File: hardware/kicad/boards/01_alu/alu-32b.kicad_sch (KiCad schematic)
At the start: 0 parts

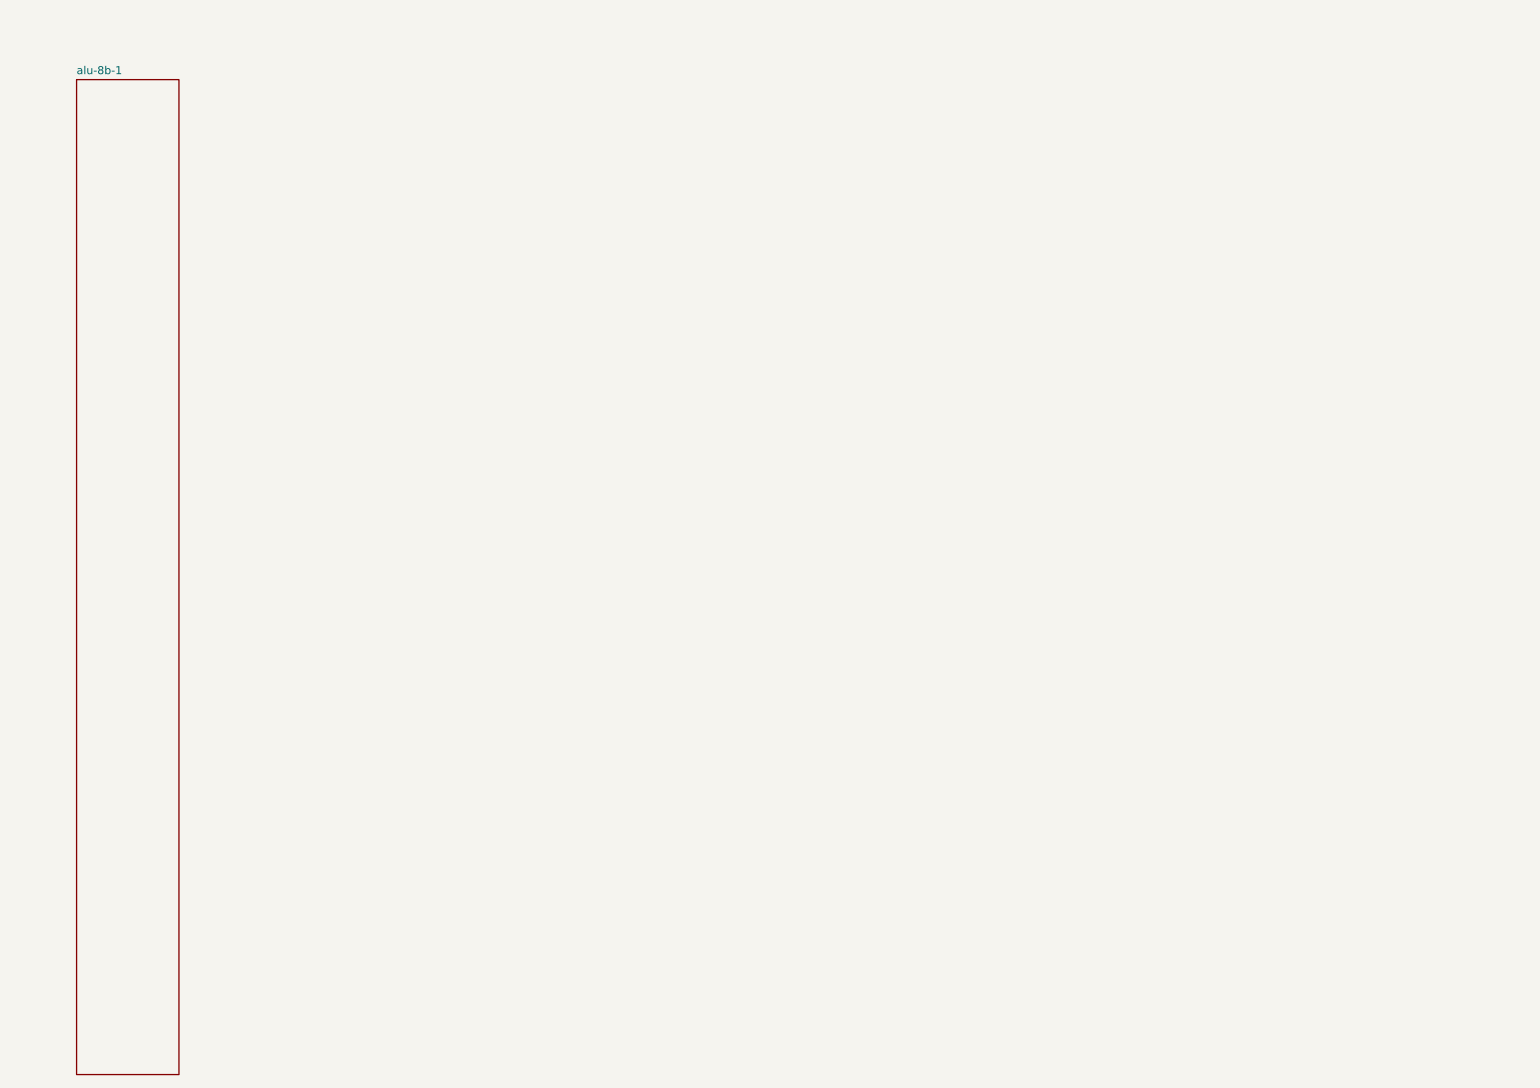
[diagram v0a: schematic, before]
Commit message: feat: designed alu0-control unit and wired on top level of 32b alu
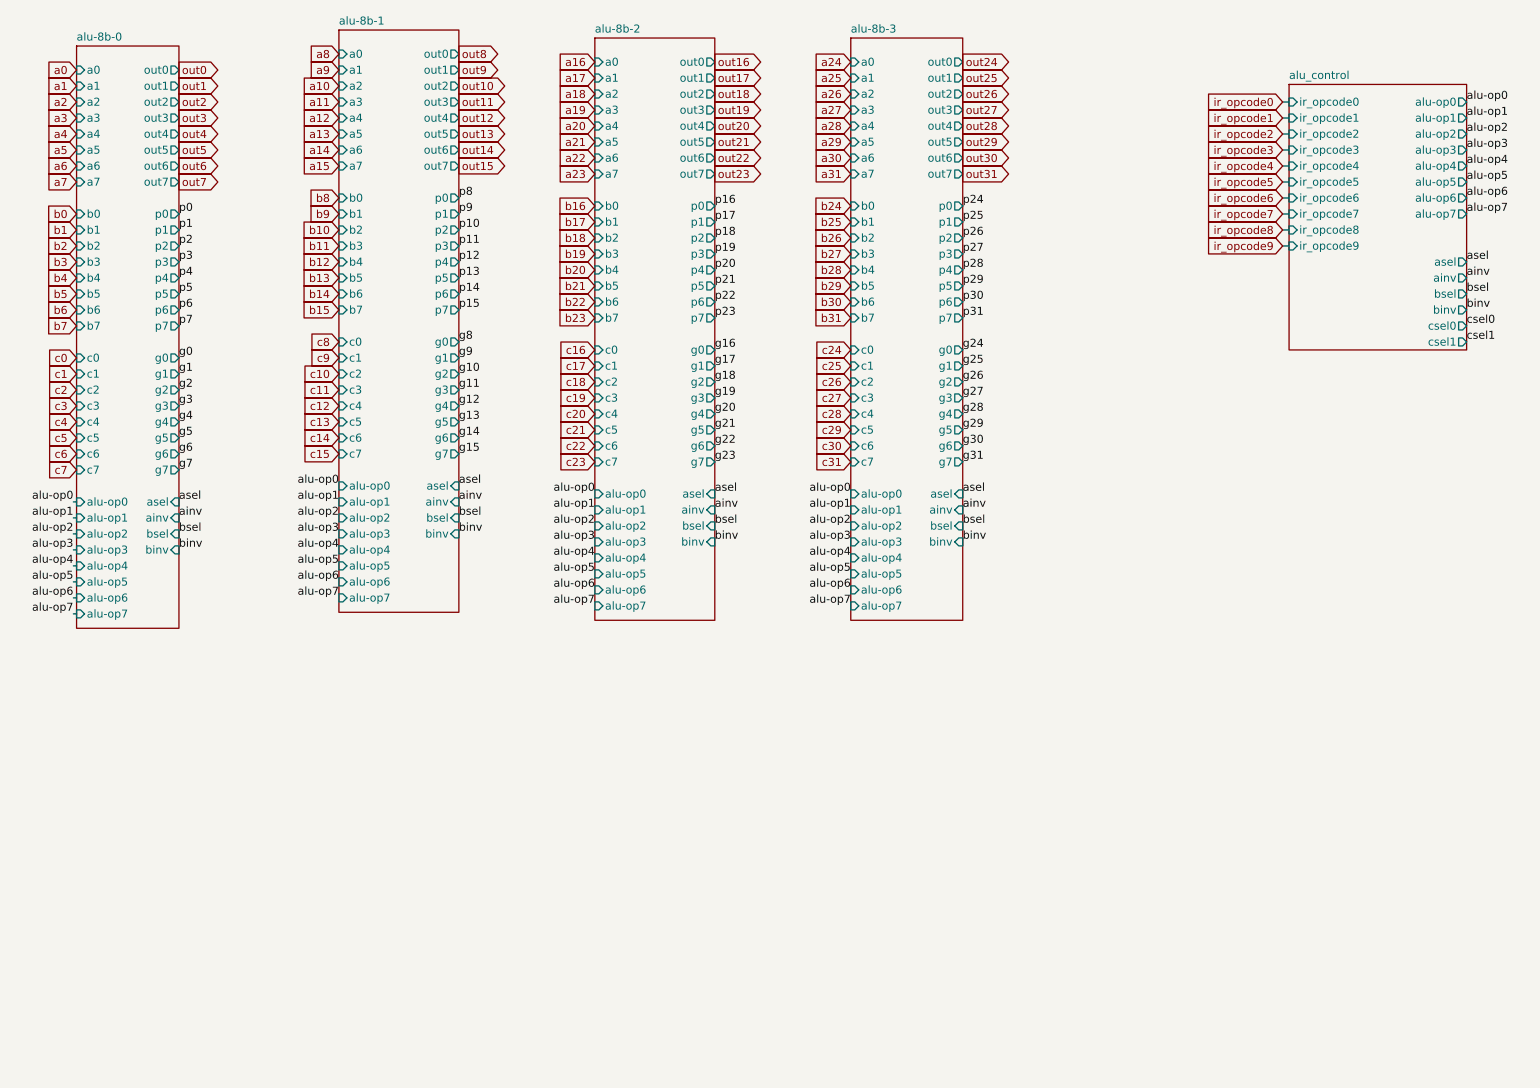
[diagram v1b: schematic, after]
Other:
- added sheet alu-8b-0 (alu-8b.kicad_sch)
- added sheet alu-8b-2 (alu-8b.kicad_sch)
- added sheet alu-8b-3 (alu-8b.kicad_sch)
- added sheet alu_control (alu_control.kicad_sch)
- sheet alu-8b-1 ports: added a0, a1, a2, a3, a4, a5, a6, a7, ainv, alu-op0, alu-op1, alu-op2, alu-op3, alu-op4, alu-op5, alu-op6, alu-op7, asel, b0, b1, b2, b3, b4, b5, b6, b7, binv, bsel, c0, c1, c2, c3, c4, c5, c6, c7, g0, g1, g2, g3, g4, g5, g6, g7, out0, out1, out2, out3, out4, out5, out6, out7, p0, p1, p2, p3, p4, p5, p6, p7; removed none

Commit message: kicad: checkpoint; designed the alu display logic; clock circuit
Added registers for each display to ensure robustness and less worry about debugging screen, keeping focus on the alu board and other components
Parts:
- added C1, C10, C11, C12, C13, C14, C15, C16, C17, C18, C19, C2, C20, C205, C206, C21, C22, C23, C24, C25, C26, C27, C28, C29, C3, C30, C4, C5, C6, C7, C8, C9: 100nF, Capacitor_SMD:C_0805_2012Metric, symbol Device:C
- added J1, J2, J3, J4: Conn_02x16_Odd_Even, Connector_PinHeader_2.54mm:PinHeader_2x16_P2.54mm_Vertical, symbol Connector_Generic:Conn_02x16_Odd_Even
- added J6: Conn_02x07_Odd_Even, Connector_PinHeader_2.54mm:PinHeader_2x07_P2.54mm_Vertical, symbol Connector_Generic:Conn_02x07_Odd_Even
- added U1, U10, U13, U14, U16, U18, U21, U4, U5, U6, U9: 74LS182, Package_DIP:DIP-16_W7.62mm, symbol 74xx:74LS182
- added U11, U12, U19, U2, U20, U27, U3, U7, U8: 74LS540, Package_SO:SOIC-20W_7.5x12.8mm_P1.27mm, symbol 74xx:74LS540
- added U15: 74LS153, Package_SO:SOIC-16_3.9x9.9mm_P1.27mm, symbol 74xx:74LS153
- added U17: 74AHCT1G08, Package_TO_SOT_SMD:SOT-23-5, symbol 74xGxx:74AHCT1G08
- added U205, U206: 74AHC541, Package_SO:SOIC-20W_7.5x12.8mm_P1.27mm, symbol 74xx:74AHC541
- added U22, U28: 74LS377, Package_SO:SOIC-20W_7.5x12.8mm_P1.27mm, symbol 74xx:74LS377
- added U23: 74HC86, Package_SO:SOIC-14_3.9x8.7mm_P1.27mm, symbol 74xx:74HC86
- added U24, U25, U29, U30: 74LS30, Package_SO:SOIC-14_3.9x8.7mm_P1.27mm, symbol 74xx:74LS30
- added U26: 74HCT00, Package_SO:SOIC-14_3.9x8.7mm_P1.27mm, symbol 74xx:74HCT00
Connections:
- net a0: now also J1.1 (Pin_1)
- net a1: now also J1.2 (Pin_2)
- net a10: now also J1.11 (Pin_11)
- net a11: now also J1.12 (Pin_12)
- net a12: now also J1.13 (Pin_13)
- net a13: now also J1.14 (Pin_14)
- net a14: now also J1.15 (Pin_15)
- net a15: now also J1.16 (Pin_16)
- net a16: now also J1.17 (Pin_17)
- net a17: now also J1.18 (Pin_18)
- net a18: now also J1.19 (Pin_19)
- net a19: now also J1.20 (Pin_20)
- net a2: now also J1.3 (Pin_3)
- net a20: now also J1.21 (Pin_21)
- net a21: now also J1.22 (Pin_22)
- net a22: now also J1.23 (Pin_23)
- net a23: now also J1.24 (Pin_24)
- net a24: now also J1.25 (Pin_25)
- net a25: now also J1.26 (Pin_26)
- net a26: now also J1.27 (Pin_27)
- net a27: now also J1.28 (Pin_28)
- net a28: now also J1.29 (Pin_29)
- net a29: now also J1.30 (Pin_30)
- net a3: now also J1.4 (Pin_4)
- net a30: now also J1.31 (Pin_31)
- net a31: now also J1.32 (Pin_32)
- net a4: now also J1.5 (Pin_5)
- net a5: now also J1.6 (Pin_6)
- net a6: now also J1.7 (Pin_7)
- net a7: now also J1.8 (Pin_8)
- net a8: now also J1.9 (Pin_9)
- net a9: now also J1.10 (Pin_10)
- net ainv: now also U205.17 (Y1)
- net alu-op0: now also U206.18 (Y0)
- net alu-op1: now also U206.17 (Y1)
- net alu-op2: now also U206.16 (Y2)
- net alu-op3: now also U206.15 (Y3)
- net alu-op4: now also U206.14 (Y4)
- net alu-op5: now also U206.13 (Y5)
- net alu-op6: now also U206.12 (Y6)
- net alu-op7: now also U206.11 (Y7)
- net asel: now also U205.18 (Y0)
- net b0: now also J3.1 (Pin_1)
- net b1: now also J3.2 (Pin_2)
- net b10: now also J3.11 (Pin_11)
- net b11: now also J3.12 (Pin_12)
- net b12: now also J3.13 (Pin_13)
- net b13: now also J3.14 (Pin_14)
- net b14: now also J3.15 (Pin_15)
- net b15: now also J3.16 (Pin_16)
- net b16: now also J3.17 (Pin_17)
- net b17: now also J3.18 (Pin_18)
- net b18: now also J3.19 (Pin_19)
- net b19: now also J3.20 (Pin_20)
- net b2: now also J3.3 (Pin_3)
- net b20: now also J3.21 (Pin_21)
- net b21: now also J3.22 (Pin_22)
- net b22: now also J3.23 (Pin_23)
- net b23: now also J3.24 (Pin_24)
- net b24: now also J3.25 (Pin_25)
- net b25: now also J3.26 (Pin_26)
- net b26: now also J3.27 (Pin_27)
- net b27: now also J3.28 (Pin_28)
- net b28: now also J3.29 (Pin_29)
- net b29: now also J3.30 (Pin_30)
- net b3: now also J3.4 (Pin_4)
- net b30: now also J3.31 (Pin_31)
- net b31: now also J3.32 (Pin_32)
- net b4: now also J3.5 (Pin_5)
- net b5: now also J3.6 (Pin_6)
- net b6: now also J3.7 (Pin_7)
- net b7: now also J3.8 (Pin_8)
- net b8: now also J3.9 (Pin_9)
- net b9: now also J3.10 (Pin_10)
- net binv: now also U205.15 (Y3)
- net bsel: now also U205.16 (Y2)
- net c0: now also J2.1 (Pin_1), U15.13 (I3b), U15.3 (I3a)
- net c1: now also J2.2 (Pin_2)
- net c10: now also J2.11 (Pin_11)
- net c11: now also J2.12 (Pin_12)
- net c12: now also J2.13 (Pin_13)
- net c13: now also J2.14 (Pin_14)
- net c14: now also J2.15 (Pin_15)
- net c15: now also J2.16 (Pin_16)
- net c16: now also J2.17 (Pin_17)
- net c17: now also J2.18 (Pin_18)
- net c18: now also J2.19 (Pin_19)
- net c19: now also J2.20 (Pin_20)
- net c2: now also J2.3 (Pin_3)
- net c20: now also J2.21 (Pin_21)
- net c21: now also J2.22 (Pin_22)
- net c22: now also J2.23 (Pin_23)
- net c23: now also J2.24 (Pin_24)
- net c24: now also J2.25 (Pin_25)
- net c25: now also J2.26 (Pin_26)
- net c26: now also J2.27 (Pin_27)
- net c27: now also J2.28 (Pin_28)
- net c28: now also J2.29 (Pin_29)
- net c29: now also J2.30 (Pin_30)
- net c3: now also J2.4 (Pin_4)
- net c30: now also J2.31 (Pin_31)
- net c31: now also J2.32 (Pin_32)
- net c4: now also J2.5 (Pin_5)
- net c5: now also J2.6 (Pin_6)
- net c6: now also J2.7 (Pin_7)
- net c7: now also J2.8 (Pin_8)
- net c8: now also J2.9 (Pin_9)
- net c9: now also J2.10 (Pin_10)
- net csel0: now also U15.14 (S0), U17.1, U205.14 (Y4)
- net csel1: now also U15.2 (S1), U17.2, U205.13 (Y5)
- net g0: now also U3.2 (A0)
- net g1: now also U3.3 (A1)
- net g10: now also U8.4 (A2)
- net g11: now also U8.5 (A3)
- net g12: now also U8.6 (A4)
- net g13: now also U8.7 (A5)
- net g14: now also U8.8 (A6)
- net g15: now also U8.9 (A7)
- net g16: now also U12.2 (A0)
- net g17: now also U12.3 (A1)
- net g18: now also U12.4 (A2)
- net g19: now also U12.5 (A3)
- net g2: now also U3.4 (A2)
- net g20: now also U12.6 (A4)
- net g21: now also U12.7 (A5)
- net g22: now also U12.8 (A6)
- net g23: now also U12.9 (A7)
- net g24: now also U20.2 (A0)
- net g25: now also U20.3 (A1)
- net g26: now also U20.4 (A2)
- net g27: now also U20.5 (A3)
- net g28: now also U20.6 (A4)
- net g29: now also U20.7 (A5)
- net g3: now also U3.5 (A3)
- net g30: now also U20.8 (A6)
- net g31: now also U20.9 (A7)
- net g4: now also U3.6 (A4)
- net g5: now also U3.7 (A5)
- net g6: now also U3.8 (A6)
- net g7: now also U3.9 (A7)
- net g8: now also U8.2 (A0)
- net g9: now also U8.3 (A1)
- net out0: now also J4.1 (Pin_1), U24.1
- net out1: now also J4.2 (Pin_2), U24.2
- net out10: now also J4.11 (Pin_11), U25.3
- net out11: now also J4.12 (Pin_12), U25.4
- net out12: now also J4.13 (Pin_13), U25.5
- net out13: now also J4.14 (Pin_14), U25.6
- net out14: now also J4.15 (Pin_15), U25.11
- net out15: now also J4.16 (Pin_16), U25.12
- net out16: now also J4.17 (Pin_17), U29.1
- net out17: now also J4.18 (Pin_18), U29.2
- net out18: now also J4.19 (Pin_19), U29.3
- net out19: now also J4.20 (Pin_20), U29.4
- net out2: now also J4.3 (Pin_3), U24.3
- net out20: now also J4.21 (Pin_21), U29.5
- net out21: now also J4.22 (Pin_22), U29.6
- net out22: now also J4.23 (Pin_23), U29.11
- net out23: now also J4.24 (Pin_24), U29.12
- net out24: now also J4.25 (Pin_25), U30.1
- net out25: now also J4.26 (Pin_26), U30.2
- net out26: now also J4.27 (Pin_27), U30.3
- net out27: now also J4.28 (Pin_28), U30.4
- net out28: now also J4.29 (Pin_29), U30.5
- net out29: now also J4.30 (Pin_30), U30.6
- net out3: now also J4.4 (Pin_4), U24.4
- net out30: now also J4.31 (Pin_31), U30.11
- net out31: now also J4.32 (Pin_32), U23.1, U27.6 (A4), U30.12
- net out4: now also J4.5 (Pin_5), U24.5
- net out5: now also J4.6 (Pin_6), U24.6
- net out6: now also J4.7 (Pin_7), U24.11
- net out7: now also J4.8 (Pin_8), U24.12
- net out8: now also J4.9 (Pin_9), U25.1
- net out9: now also J4.10 (Pin_10), U25.2
- net p0: now also U2.2 (A0)
- net p1: now also U2.3 (A1)
- net p10: now also U7.4 (A2)
- net p11: now also U7.5 (A3)
- net p12: now also U7.6 (A4)
- net p13: now also U7.7 (A5)
- net p14: now also U7.8 (A6)
- net p15: now also U7.9 (A7)
- net p16: now also U11.2 (A0)
- net p17: now also U11.3 (A1)
- net p18: now also U11.4 (A2)
- net p19: now also U11.5 (A3)
- net p2: now also U2.4 (A2)
- net p20: now also U11.6 (A4)
- net p21: now also U11.7 (A5)
- net p22: now also U11.8 (A6)
- net p23: now also U11.9 (A7)
- net p24: now also U19.2 (A0)
- net p25: now also U19.3 (A1)
- net p26: now also U19.4 (A2)
- net p27: now also U19.5 (A3)
- net p28: now also U19.6 (A4)
- net p29: now also U19.7 (A5)
- net p3: now also U2.5 (A3)
- net p30: now also U19.8 (A6)
- net p31: now also U19.9 (A7)
- net p4: now also U2.6 (A4)
- net p5: now also U2.7 (A5)
- net p6: now also U2.8 (A6)
- net p7: now also U2.9 (A7)
- net p8: now also U7.2 (A0)
- net p9: now also U7.3 (A1)
- new net: U26.3, U26.9
- new net: U26.10, U26.6
- new net GND: C1.1, C10.1, C11.1, C12.1, C13.1, C14.1, C15.1, C16.1, C17.1, C18.1, C19.1, C2.1, C20.1, C205.1, C206.1, C21.1, C22.1, C23.1, C24.1, C25.1, C26.1, C27.1, C28.1, C29.1, C3.1, C30.1, C4.1, C5.1, C6.1, C7.1, C8.1, C9.1, U1.8 (GND), U10.8 (GND), U11.1 (G1), U11.10 (GND), U11.19 (G2), U12.1 (G1), U12.10 (GND), U12.19 (G2), U13.8 (GND), U14.8 (GND), U15.1 (Ea), U15.10 (I0b), U15.15 (Eb), U15.6 (I0a), U15.8 (GND), U16.14 (G2), U16.15 (P2), U16.5 (G3), U16.6 (P3), U16.8 (GND), U17.3 (GND), U18.8 (GND), U19.1 (G1), U19.10 (GND), U19.19 (G2), U2.1 (G1), U2.10 (GND), U2.19 (G2), U20.1 (G1), U20.10 (GND), U20.19 (G2), U205.1 (G1), U205.19 (G2), U206.1 (G1), U206.10 (GND), U206.19 (G2), U21.8 (GND), U22.1 (~{E}), U22.10 (GND), U22.14 (D5), U22.17 (D6), U22.18 (D7), U23.7 (GND), U24.7 (GND), U25.7 (GND), U26.7 (GND), U27.1 (G1), U27.10 (GND), U27.19 (G2), U28.1 (~{E}), U28.10 (GND), U29.7 (GND), U3.1 (G1), U3.10 (GND), U3.19 (G2), U30.7 (GND), U4.8 (GND), U5.8 (GND), U6.8 (GND), U7.1 (G1), U7.10 (GND), U7.19 (G2), U8.1 (G1), U8.10 (GND), U8.19 (G2), U9.8 (GND)
- new net VCC: C1.2, C10.2, C11.2, C12.2, C13.2, C14.2, C15.2, C16.2, C17.2, C18.2, C19.2, C2.2, C20.2, C205.2, C206.2, C21.2, C22.2, C23.2, C24.2, C25.2, C26.2, C27.2, C28.2, C29.2, C3.2, C30.2, C4.2, C5.2, C6.2, C7.2, C8.2, C9.2, U1.16 (VCC), U10.16 (VCC), U11.20 (VCC), U12.20 (VCC), U13.16 (VCC), U14.16 (VCC), U15.11 (I1b), U15.16 (VCC), U15.5 (I1a), U16.16 (VCC), U17.5 (VCC), U18.16 (VCC), U19.20 (VCC), U2.20 (VCC), U20.20 (VCC), U205.20 (VCC), U206.20 (VCC), U21.16 (VCC), U22.20 (VCC), U23.14 (VCC), U24.14 (VCC), U25.14 (VCC), U26.14 (VCC), U27.20 (VCC), U28.20 (VCC), U29.14 (VCC), U3.20 (VCC), U30.14 (VCC), U4.16 (VCC), U5.16 (VCC), U6.16 (VCC), U7.20 (VCC), U8.20 (VCC), U9.16 (VCC)
- new net ceff0: U1.13 (Cn), U15.7 (Za), U15.9 (Zb), U16.13 (Cn), U5.13 (Cn)
- new net cin-sel: U17.4
- new net clk: U205.11 (Y7), U205.12 (Y6), U22.11 (CP), U28.11 (CP)
- new net cout: U28.13 (D4)
- new net cout1: U5.12 (Cn+x)
- new net cout10: U14.11 (Cn+y)
- new net cout11: U14.9 (Cn+z)
- new net cout12: U1.9 (Cn+z), U21.13 (Cn)
- new net cout13: U21.12 (Cn+x)
- new net cout14: U21.11 (Cn+y)
- new net cout15: U21.9 (Cn+z)
- new net cout16: U10.13 (Cn), U16.12 (Cn+x), U4.13 (Cn)
- new net cout17: U4.12 (Cn+x)
- new net cout18: U4.11 (Cn+y)
- new net cout19: U4.9 (Cn+z)
- new net cout2: U5.11 (Cn+y)
- new net cout20: U10.12 (Cn+x), U6.13 (Cn)
- new net cout21: U6.12 (Cn+x)
- new net cout22: U6.11 (Cn+y)
- new net cout23: U6.9 (Cn+z)
- new net cout24: U10.11 (Cn+y), U13.13 (Cn)
- new net cout25: U13.12 (Cn+x)
- new net cout26: U13.11 (Cn+y)
- new net cout27: U13.9 (Cn+z)
- new net cout28: U10.9 (Cn+z), U18.13 (Cn)
- new net cout29: U18.12 (Cn+x)
- new net cout3: U5.9 (Cn+z)
- new net cout30: U18.11 (Cn+y)
- new net cout31: U18.9 (Cn+z), U23.4
- new net cout32: U16.11 (Cn+y), U23.5, U27.3 (A1)
- new net cout4: U1.12 (Cn+x), U9.13 (Cn)
- new net cout5: U9.12 (Cn+x)
- new net cout6: U9.11 (Cn+y)
- new net cout7: U9.9 (Cn+z)
- new net cout8: U1.11 (Cn+y), U14.13 (Cn)
- new net cout9: U14.12 (Cn+x)
- new net flagC: J6.5 (Pin_5), U15.12 (I2b), U15.4 (I2a), U28.12 (Q4)
- new net flagGT: J6.11 (Pin_11), U22.6 (Q2)
- new net flagGTE: J6.12 (Pin_12), U22.9 (Q3)
- new net flagLT: J6.9 (Pin_9), U22.2 (Q0)
- new net flagLTE: J6.10 (Pin_10), U22.5 (Q1)
- new net flagN: J6.3 (Pin_3), U28.6 (Q2)
- new net flagV: J6.7 (Pin_7), U28.16 (Q6)
- new net flagWE: U27.7 (A5)
- new net flagZ: J6.1 (Pin_1), U28.2 (Q0)
- new net g-out-0: U1.3 (G0), U5.10 (G)
- new net g-out-1: U1.1 (G1), U9.10 (G)
- new net g-out-2: U1.14 (G2), U14.10 (G)
- new net g-out-3: U1.5 (G3), U21.10 (G)
- new net g-out-4: U10.3 (G0), U4.10 (G)
- new net g-out-5: U10.1 (G1), U6.10 (G)
- new net g-out-6: U10.14 (G2), U13.10 (G)
- new net g-out-7: U10.5 (G3), U18.10 (G)
- new net g-out-A: U1.10 (G), U16.3 (G0)
- new net g-out-B: U10.10 (G), U16.1 (G1)
- new net gb0: U3.18 (Y0), U5.3 (G0)
- new net gb1: U3.17 (Y1), U5.1 (G1)
- new net gb10: U14.14 (G2), U8.16 (Y2)
- new net gb11: U14.5 (G3), U8.15 (Y3)
- new net gb12: U21.3 (G0), U8.14 (Y4)
- new net gb13: U21.1 (G1), U8.13 (Y5)
- new net gb14: U21.14 (G2), U8.12 (Y6)
- new net gb15: U21.5 (G3), U8.11 (Y7)
- new net gb16: U12.18 (Y0), U4.3 (G0)
- new net gb17: U12.17 (Y1), U4.1 (G1)
- new net gb18: U12.16 (Y2), U4.14 (G2)
- new net gb19: U12.15 (Y3), U4.5 (G3)
- new net gb2: U3.16 (Y2), U5.14 (G2)
- new net gb20: U12.14 (Y4), U6.3 (G0)
- new net gb21: U12.13 (Y5), U6.1 (G1)
- new net gb22: U12.12 (Y6), U6.14 (G2)
- new net gb23: U12.11 (Y7), U6.5 (G3)
- new net gb24: U13.3 (G0), U20.18 (Y0)
- new net gb25: U13.1 (G1), U20.17 (Y1)
- new net gb26: U13.14 (G2), U20.16 (Y2)
- new net gb27: U13.5 (G3), U20.15 (Y3)
- new net gb28: U18.3 (G0), U20.14 (Y4)
- new net gb29: U18.1 (G1), U20.13 (Y5)
- new net gb3: U3.15 (Y3), U5.5 (G3)
- new net gb30: U18.14 (G2), U20.12 (Y6)
- new net gb31: U18.5 (G3), U20.11 (Y7)
- new net gb4: U3.14 (Y4), U9.3 (G0)
- new net gb5: U3.13 (Y5), U9.1 (G1)
- new net gb6: U3.12 (Y6), U9.14 (G2)
- new net gb7: U3.11 (Y7), U9.5 (G3)
- new net gb8: U14.3 (G0), U8.18 (Y0)
- new net gb9: U14.1 (G1), U8.17 (Y1)
- new net gt-sign: U22.7 (D2), U26.11, U27.8 (A6)
- new net gte-sign: U22.8 (D3), U27.15 (Y3)
- new net lt-sign: U22.3 (D0), U23.3, U26.12, U27.5 (A3)
- new net lte-sign: U22.4 (D1), U27.12 (Y6)
- new net nand0: U24.8, U26.1
- new net nand1: U25.8, U26.2
- new net nand2: U26.4, U29.8
- new net nand3: U26.5, U30.8
- new net nout: U28.7 (D2)
- new net p-out-0: U1.4 (P0), U5.7 (P)
- new net p-out-1: U1.2 (P1), U9.7 (P)
- new net p-out-2: U1.15 (P2), U14.7 (P)
- new net p-out-3: U1.6 (P3), U21.7 (P)
- new net p-out-4: U10.4 (P0), U4.7 (P)
- new net p-out-5: U10.2 (P1), U6.7 (P)
- new net p-out-6: U10.15 (P2), U13.7 (P)
- new net p-out-7: U10.6 (P3), U18.7 (P)
- new net p-out-A: U1.7 (P), U16.4 (P0)
- new net p-out-B: U10.7 (P), U16.2 (P1)
- new net pb0: U2.18 (Y0), U5.4 (P0)
- new net pb1: U2.17 (Y1), U5.2 (P1)
- new net pb10: U14.15 (P2), U7.16 (Y2)
- new net pb11: U14.6 (P3), U7.15 (Y3)
- new net pb12: U21.4 (P0), U7.14 (Y4)
- new net pb13: U21.2 (P1), U7.13 (Y5)
- new net pb14: U21.15 (P2), U7.12 (Y6)
- new net pb15: U21.6 (P3), U7.11 (Y7)
- new net pb16: U11.18 (Y0), U4.4 (P0)
- new net pb17: U11.17 (Y1), U4.2 (P1)
- new net pb18: U11.16 (Y2), U4.15 (P2)
- new net pb19: U11.15 (Y3), U4.6 (P3)
- new net pb2: U2.16 (Y2), U5.15 (P2)
- new net pb20: U11.14 (Y4), U6.4 (P0)
- new net pb21: U11.13 (Y5), U6.2 (P1)
- new net pb22: U11.12 (Y6), U6.15 (P2)
- new net pb23: U11.11 (Y7), U6.6 (P3)
- new net pb24: U13.4 (P0), U19.18 (Y0)
- new net pb25: U13.2 (P1), U19.17 (Y1)
- new net pb26: U13.15 (P2), U19.16 (Y2)
- new net pb27: U13.6 (P3), U19.15 (Y3)
- new net pb28: U18.4 (P0), U19.14 (Y4)
- new net pb29: U18.2 (P1), U19.13 (Y5)
- new net pb3: U2.15 (Y3), U5.6 (P3)
- new net pb30: U18.15 (P2), U19.12 (Y6)
- new net pb31: U18.6 (P3), U19.11 (Y7)
- new net pb4: U2.14 (Y4), U9.4 (P0)
- new net pb5: U2.13 (Y5), U9.2 (P1)
- new net pb6: U2.12 (Y6), U9.15 (P2)
- new net pb7: U2.11 (Y7), U9.6 (P3)
- new net pb8: U14.4 (P0), U7.18 (Y0)
- new net pb9: U14.2 (P1), U7.17 (Y1)
- new net vout: U23.2, U23.6, U27.4 (A2), U28.17 (D6)
- new net zout: U26.13, U26.8, U27.2 (A0), U28.3 (D0)
- new net ~AisZero: U22.13 (D4)
- new net ~cout: U27.17 (Y1), U28.14 (D5)
- new net ~flagAisZero: U22.12 (Q4)
- new net ~flagC: J6.6 (Pin_6), U28.15 (Q5)
- new net ~flagN: J6.4 (Pin_4), U28.9 (Q3)
- new net ~flagV: J6.8 (Pin_8), U28.19 (Q7)
- new net ~flagWE: U27.13 (Y5)
- new net ~flagZ: J6.2 (Pin_2), U28.5 (Q1)
- new net ~nout: U27.14 (Y4), U28.8 (D3)
- new net ~vout: U27.16 (Y2), U28.18 (D7)
- new net ~zout: U27.18 (Y0), U28.4 (D1)
- no-connect marks 0 -> 17
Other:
- added sheet display (alu-display.kicad_sch)
- added sheet drive8_2to1-0 (../../modules/mux/drivers-74xx/drive8_2to1.kicad_sch)
- added sheet drive8_2to1-1 (../../modules/mux/drivers-74xx/drive8_2to1.kicad_sch)
- added sheet drive8_2to1-2 (../../modules/mux/drivers-74xx/drive8_2to1.kicad_sch)
- added sheet drive8_2to1-3 (../../modules/mux/drivers-74xx/drive8_2to1.kicad_sch)

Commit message: alu: completed all core schematics; DRC and ERC pending 🎉
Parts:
- removed C205, C206: 100nF, Capacitor_SMD:C_0805_2012Metric, symbol Device:C
- removed J6: Conn_02x07_Odd_Even, Connector_PinHeader_2.54mm:PinHeader_2x07_P2.54mm_Vertical, symbol Connector_Generic:Conn_02x07_Odd_Even
- removed U205, U206: 74AHC541, Package_SO:SOIC-20W_7.5x12.8mm_P1.27mm, symbol 74xx:74AHC541
- added C171, C172: C, Capacitor_SMD:C_0805_2012Metric, symbol Device:C
- added J1: Conn_02x06_Odd_Even, Connector_PinHeader_2.54mm:PinHeader_2x06_P2.54mm_Vertical, symbol Connector_Generic:Conn_02x06_Odd_Even
- added J6: Conn_02x05_Odd_Even, Connector_PinHeader_2.54mm:PinHeader_2x05_P2.54mm_Vertical, symbol Connector_Generic:Conn_02x05_Odd_Even
- added U299, U300: 74AHC541, Package_SO:SOIC-20W_7.5x12.8mm_P1.27mm, symbol 74xx:74AHC541
- renumbered C25 to C26, C26 to C27, C27 to C28, C28 to C29, C29 to C30, C30 to C32, J1 to J2, J2 to J3, J3 to J4, J4 to J5, U27 to U28, U28 to U29, U29 to U30, U30 to U31
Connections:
- net ~AisZero is gone; now on net GND: U22.13 (D4)
- net GND: now also C171.1, C172.1, U299.1 (G1), U299.10 (GND), U299.19 (G2), U300.1 (G1), U300.10 (GND), U300.19 (G2); no longer U15.6 (I0a)
- net VCC: now also C171.2, C172.2, U299.20 (VCC), U300.20 (VCC); no longer U15.5 (I1a)
- net c0: no longer U15.3 (I3a)
- net ceff0: no longer U15.7 (Za)
- net flagC: now also J1.5 (Pin_5); no longer U15.4 (I2a)
- net flagGT: now also J1.11 (Pin_11)
- net flagGTE: now also J1.12 (Pin_12)
- net flagLT: now also J1.9 (Pin_9)
- net flagLTE: now also J1.10 (Pin_10)
- net flagN: now also J1.3 (Pin_3)
- net flagV: now also J1.7 (Pin_7)
- net flagZ: now also J1.1 (Pin_1)
- net ~flagC: now also J1.6 (Pin_6)
- net ~flagN: now also J1.4 (Pin_4)
- net ~flagV: now also J1.8 (Pin_8)
- net ~flagZ: now also J1.2 (Pin_2)
- net ~flagAisZero: no longer names the net of U22.12 (Q4)
- new net: J6.1 (Pin_1), U299.2 (A0)
- new net: J6.3 (Pin_3), U299.3 (A1)
- new net: J6.5 (Pin_5), U299.4 (A2)
- new net: J6.7 (Pin_7), U299.5 (A3)
- new net: J6.9 (Pin_9), U299.6 (A4)
- new net: J6.2 (Pin_2), U300.2 (A0)
- new net: J6.4 (Pin_4), U300.3 (A1)
- new net: J6.6 (Pin_6), U300.4 (A2)
- new net: J6.8 (Pin_8), U300.5 (A3)
- new net: J6.10 (Pin_10), U300.6 (A4)
- new net ir-opcode0: U299.18 (Y0)
- new net ir-opcode1: U300.18 (Y0)
- new net ir-opcode2: U299.17 (Y1)
- new net ir-opcode3: U300.17 (Y1)
- new net ir-opcode4: U299.16 (Y2)
- new net ir-opcode5: U300.16 (Y2)
- new net ir-opcode6: U299.15 (Y3)
- new net ir-opcode7: U300.15 (Y3)
- new net ir-opcode8: U299.14 (Y4)
- new net ir-opcode9: U300.14 (Y4)
- no-connect marks 17 -> 35
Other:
- sheet alu_control ports: added none; removed ainv, alu-op0, alu-op1, alu-op2, alu-op3, alu-op4, alu-op5, alu-op6, alu-op7, asel, binv, bsel, csel0, csel1, ir_opcode0, ir_opcode1, ir_opcode2, ir_opcode3, ir_opcode4, ir_opcode5, ir_opcode6, ir_opcode7, ir_opcode8, ir_opcode9

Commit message: refactor: improved global labeling and reduced ERC from 300+ to 6 power flags and minor connector in errors
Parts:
- added J7: Conn_02x04_Odd_Even, Connector_PinHeader_2.54mm:PinHeader_2x04_P2.54mm_Vertical, symbol Connector_Generic:Conn_02x04_Odd_Even
- J1: footprint Connector_PinHeader_2.54mm:PinHeader_2x06_P2.54mm_Vertical -> Connector_PinSocket_2.54mm:PinSocket_2x06_P2.54mm_Vertical
- J6: renamed from J5; footprint Connector_PinHeader_2.54mm:PinHeader_2x16_P2.54mm_Vertical -> Connector_PinSocket_2.54mm:PinSocket_2x16_P2.54mm_Vertical
- renumbered C2 to C1, C17 to C16, C16 to C17, C19 to C18, C18 to C19, C3 to C2, C26 to C25, C27 to C26, C28 to C27, C171 to C28, C4 to C3, C172 to C31, C1 to C4, C7 to C6, C6 to C7, J6 to J2, J2 to J3, J3 to J4, J4 to J5, U2 to U1, U17 to U16, U16 to U17, U19 to U18, U18 to U19, U3 to U2, U28 to U27, U29 to U28, U30 to U29, U4 to U3, U31 to U30, U299 to U31, U300 to U32, U1 to U4, U7 to U6, U6 to U7
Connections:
- net clk is gone; now on net sys-clk: U22.11 (CP), U28.11 (CP)
- net GND: now also J7.2 (Pin_2), J7.4 (Pin_4), J7.6 (Pin_6); no longer U22.1 (~{E}), U28.1 (~{E})
- net VCC: now also J7.1 (Pin_1), J7.3 (Pin_3), J7.5 (Pin_5)
- net ~flagWE: now also U22.1 (~{E}), U28.1 (~{E})
- net sys-clk: now reaches U31.11 (Y7)
- net sys-clk: now also U31.12 (Y6), U31.13 (Y5), U32.11 (Y7), U32.12 (Y6), U32.13 (Y5)
- net at U31.7 (A5): now also U31.8 (A6), U31.9 (A7), J7.7 (Pin_7)
- net at U32.7 (A5): now also U32.8 (A6), U32.9 (A7), J7.8 (Pin_8)
- no-connect marks 35 -> 23
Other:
- sheet alu-8b-0 ports: added none; removed ainv, alu-op0, alu-op1, alu-op2, alu-op3, alu-op4, alu-op5, alu-op6, alu-op7, asel, binv, bsel
- sheet alu-8b-1 ports: added none; removed ainv, alu-op0, alu-op1, alu-op2, alu-op3, alu-op4, alu-op5, alu-op6, alu-op7, asel, binv, bsel
- sheet alu-8b-2 ports: added none; removed ainv, alu-op0, alu-op1, alu-op2, alu-op3, alu-op4, alu-op5, alu-op6, alu-op7, asel, binv, bsel
- sheet alu-8b-3 ports: added none; removed ainv, alu-op0, alu-op1, alu-op2, alu-op3, alu-op4, alu-op5, alu-op6, alu-op7, asel, binv, bsel
- sheet display: file alu-display.kicad_sch -> display-counter.kicad_sch
- moved on the sheet: C1, C10, C11, C12, C13, C14, C17, C18, C19, C2, C20, C21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

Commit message: fix: fixed erc to 0; remaining are warnings about labeling which are being fixed; latest alu schematics pending decoration and organization
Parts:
- renumbered C32 to C31, C31 to C32, J7 to J3, J3 to J4, J4 to J5, J5 to J6, J6 to J7
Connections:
- net cout is gone; now on net cout32: U28.13 (D4)
- net out31 is gone; now on net nout: J7.32 (Pin_32), U23.1, U27.6 (A4), U30.12
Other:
- sheet alu_control: file alu_control.kicad_sch -> alu-control.kicad_sch
- sheet display: file display-counter.kicad_sch -> alu-display.kicad_sch

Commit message: refactor: placing buses in design across alu to improve readability and debugging
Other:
- added sheet drive_inv32 (drive_inv32.kicad_sch)
- sheet alu-8b-0 ports: added a_slice[7..0], b_slice[7..0], c_slice[7..0], g_slice[7..0], out_slice[7..0], p_slice[7..0]; removed a0, a1, a2, a3, a4, a5, a6, a7, b0, b1, b2, b3, b4, b5, b6, b7, c0, c1, c2, c3, c4, c5, c6, c7, g0, g1, g2, g3, g4, g5, g6, g7, out0, out1, out2, out3, out4, out5, out6, out7, p0, p1, p2, p3, p4, p5, p6, p7
- sheet alu-8b-1 ports: added a_slice[7..0], b_slice[7..0], c_slice[7..0], g_slice[7..0], out_slice[7..0], p_slice[7..0]; removed a0, a1, a2, a3, a4, a5, a6, a7, b0, b1, b2, b3, b4, b5, b6, b7, c0, c1, c2, c3, c4, c5, c6, c7, g0, g1, g2, g3, g4, g5, g6, g7, out0, out1, out2, out3, out4, out5, out6, out7, p0, p1, p2, p3, p4, p5, p6, p7
- sheet alu-8b-2 ports: added a_slice[7..0], b_slice[7..0], c_slice[7..0], g_slice[7..0], out_slice[7..0], p_slice[7..0]; removed a0, a1, a2, a3, a4, a5, a6, a7, b0, b1, b2, b3, b4, b5, b6, b7, c0, c1, c2, c3, c4, c5, c6, c7, g0, g1, g2, g3, g4, g5, g6, g7, out0, out1, out2, out3, out4, out5, out6, out7, p0, p1, p2, p3, p4, p5, p6, p7
- sheet alu-8b-3 ports: added a_slice[7..0], b_slice[7..0], c_slice[7..0], g_slice[7..0], out_slice[7..0], p_slice[7..0]; removed a0, a1, a2, a3, a4, a5, a6, a7, b0, b1, b2, b3, b4, b5, b6, b7, c0, c1, c2, c3, c4, c5, c6, c7, g0, g1, g2, g3, g4, g5, g6, g7, out0, out1, out2, out3, out4, out5, out6, out7, p0, p1, p2, p3, p4, p5, p6, p7
